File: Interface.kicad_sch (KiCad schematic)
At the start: 4 parts, among them Q1 AO3401A

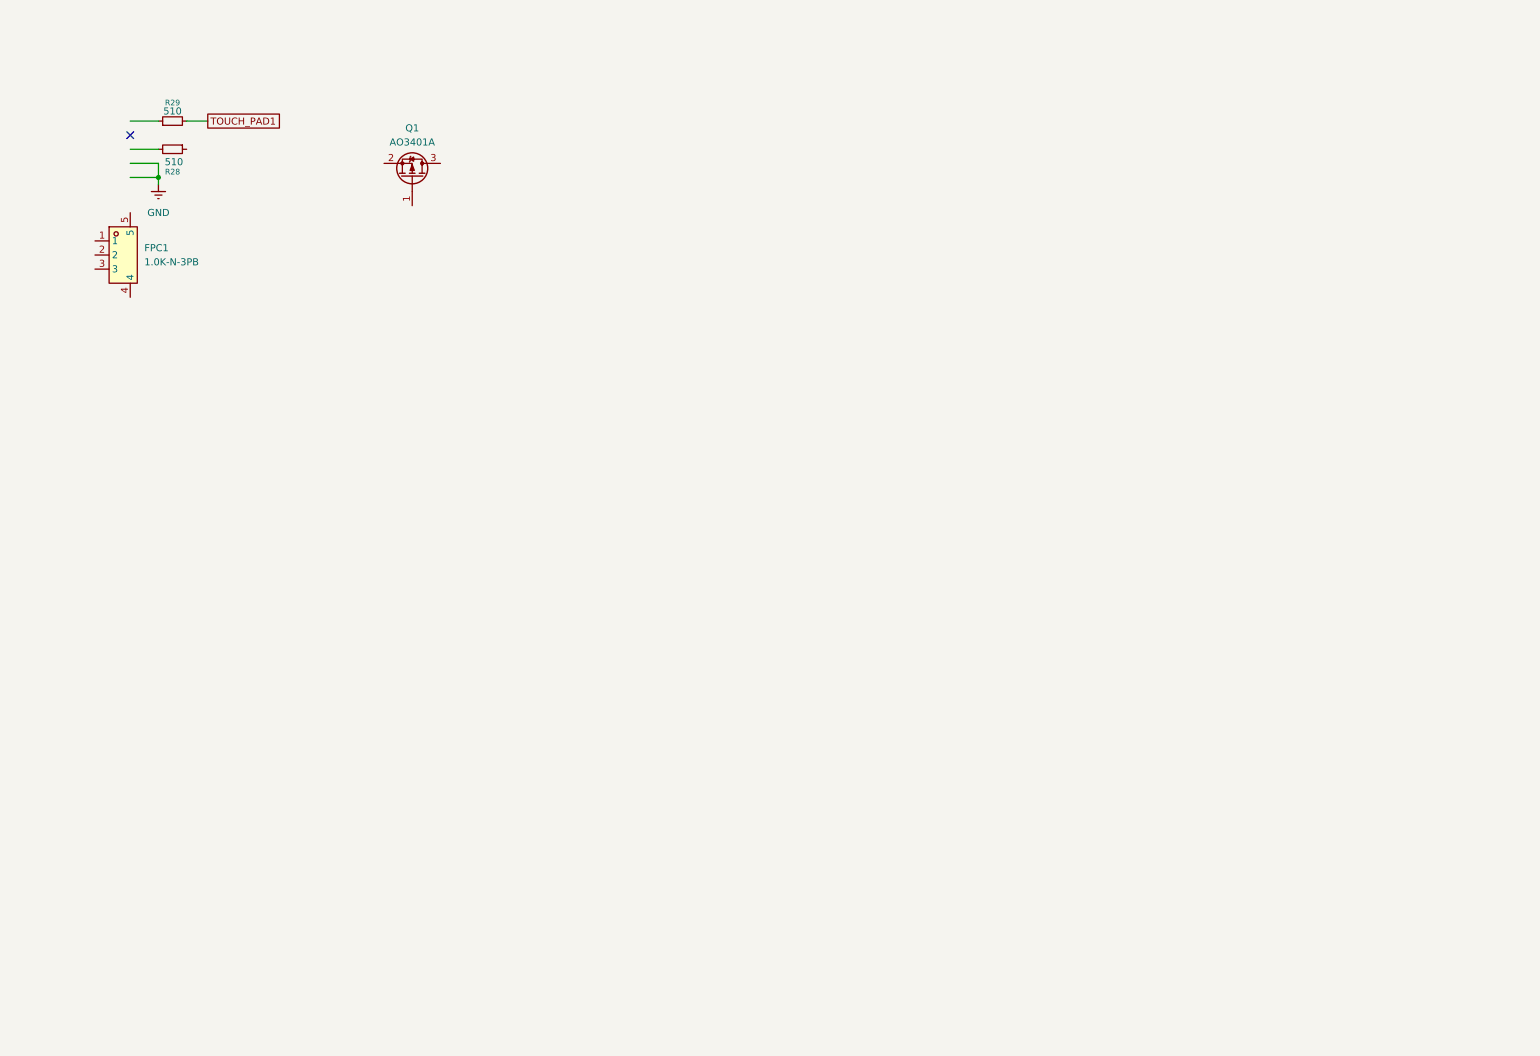
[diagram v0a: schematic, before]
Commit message: done interfacePage
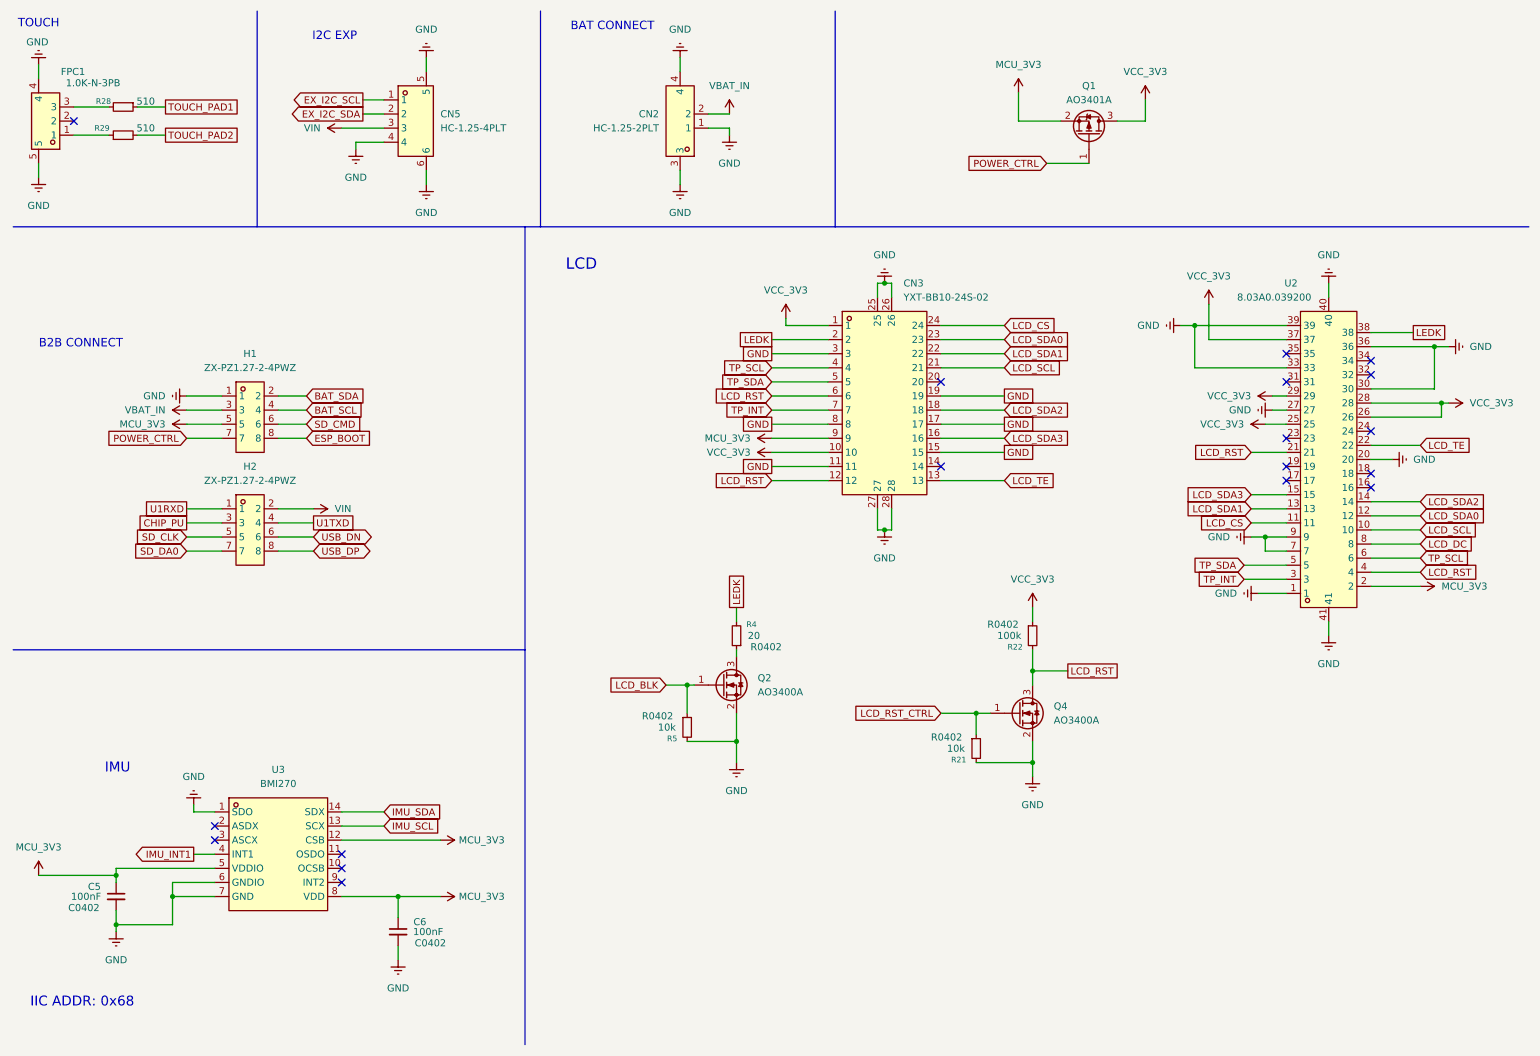
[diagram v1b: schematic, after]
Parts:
- added C5, C6: 100nF, C0402, symbol Device:C_Small
- added CN2: HC-1.25-2PLT, echoEarCustomFootprint:CONN-SMD_HC-1.25-2PLT, symbol CONN_HEADER_SMD_2POS_1_25mm_HC_1_25_2PTL:HC-1.25-2PLT
- added CN3: YXT-BB10-24S-02, echoEarCustomFootprint:CONN-SMD_YXT-BB10-24S-02, symbol YXT-BB10-24S-02_CONN_BoardToBoard_24POS_SMD:YXT-BB10-24S-02
- added CN5: HC-1.25-4PLT, echoEarCustomFootprint:CONN-SMD_4P-P1.25_HCTL_HC-1.25-4PLT, symbol CONN_HEADER_SMD_4POS_1.25mm_HC-1_25_4PLT:HC-1.25-4PLT
- added H1, H2: ZX-PZ1.27-2-4PWZ, echoEarCustomFootprint:HDR-SMD_8P-P1.27-LS5.5_ZX-PZ1.27-2-4PWZ, symbol ZX-PZ1.27-2-4PWZ:ZX-PZ1.27-2-4PWZ
- added Q2, Q4: AO3400A, Package_TO_SOT_SMD:SOT-23, symbol Transistor_FET:AO3400A
- added R21, R5: 10k, R0402, symbol Device:R_Small
- added R22: 100k, R0402, symbol Device:R_Small
- added R4: 20, R0402, symbol Device:R_Small
- added U2: 8.03A0.039200, echoEarCustomFootprint:FPC-SMD_39P-P0.60_DIANWEI_8.03A0.039200, symbol 8.03A0.039200:8.03A0.039200
- added U3: BMI270, echoEarCustomFootprint:BMI270, symbol BMI270_motionSensor_IMU:BMI270
- FPC1: footprint easyeda2kicad:FPC-SMD_3P-P1.00_HDGC_1.0K-N-3PB -> echoEarCustomFootprint:FPC-SMD_3P-P1.00_HDGC_1.0K-N-3PB
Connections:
- net GND: now also FPC1.4, FPC1.5, C5.2, C6.2, CN2.1, CN2.3, CN2.4, CN3.11, CN3.15, CN3.17, CN3.19, CN3.25, CN3.26, CN3.27, CN3.28, CN3.3, CN3.8, CN5.4, CN5.5, CN5.6, H1.1, Q2.2 (S), Q4.2 (S), R21.2, R5.2, U2.1, U2.20, U2.27, U2.30, U2.33, U2.36, U2.39, U2.40, U2.41, U2.7, U2.9, U3.1 (SDO), U3.6 (GNDIO), U3.7 (GND)
- net TOUCH_PAD1: now also R28.1; no longer R29.2
- net at FPC1.1: now also R29.1
- net at FPC1.3: now also R28.2
- net POWER_CTRL: now reaches Q1.1 (G)
- net POWER_CTRL: now also H1.7
- net MCU_3V3: now reaches Q1.2 (S)
- net MCU_3V3: now also C5.1, C6.1, CN3.9, H1.5, U2.2, U3.12 (CSB), U3.5 (VDDIO), U3.8 (VDD)
- net VCC_3V3: now reaches Q1.3 (D)
- net VCC_3V3: now also CN3.1, CN3.10, R22.1, U2.25, U2.26, U2.28, U2.29, U2.37
- new net: Q2.3 (D), R4.1
- new net BAT_SCL: H1.4
- new net BAT_SDA: H1.2
- new net CHIP_PU: H2.3
- new net ESP_BOOT: H1.8
- new net EX_I2C_SCL: CN5.1
- new net EX_I2C_SDA: CN5.2
- new net IMU_INT1: U3.4 (INT1)
- new net IMU_SCL: U3.13 (SCX)
- new net IMU_SDA: U3.14 (SDX)
- new net LCD_BLK: Q2.1 (G), R5.1
- new net LCD_CS: CN3.24, U2.11
- new net LCD_DC: U2.8
- new net LCD_RST: CN3.12, CN3.6, Q4.3 (D), R22.2, U2.21, U2.4
- new net LCD_RST_CTRL: Q4.1 (G), R21.1
- new net LCD_SCL: CN3.21, U2.10
- new net LCD_SDA0: CN3.23, U2.12
- new net LCD_SDA1: CN3.22, U2.13
- new net LCD_SDA2: CN3.18, U2.14
- new net LCD_SDA3: CN3.16, U2.15
- new net LCD_TE: CN3.13, U2.22
- new net LEDK: CN3.2, R4.2, U2.38
- new net SD_CLK: H2.5
- new net SD_CMD: H1.6
- new net SD_DA0: H2.7
- new net TOUCH_PAD2: R29.2
- new net TP_INT: CN3.7, U2.3
- new net TP_SCL: CN3.4, U2.6
- new net TP_SDA: CN3.5, U2.5
- new net U1RXD: H2.1
- new net U1TXD: H2.4
- new net USB_DN: H2.6
- new net USB_DP: H2.8
- new net VBAT_IN: CN2.2, H1.3
- new net VIN: CN5.3, H2.2
- no-connect marks 1 -> 18
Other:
- note added: "B2B CONNECT"
- note added: "BAT CONNECT"
- note added: "I2C EXP"
- note added: "IIC ADDR: 0x68"
- note added: "IMU"
- note added: "LCD"
- note added: "TOUCH"
- title: (none) -> Interface
- moved on the sheet: FPC1, Q1, R28, R29
